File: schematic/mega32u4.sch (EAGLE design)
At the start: 28 parts, among them Q1 16 MHz, T1 BC847, X1 MINI-USB-32005-201

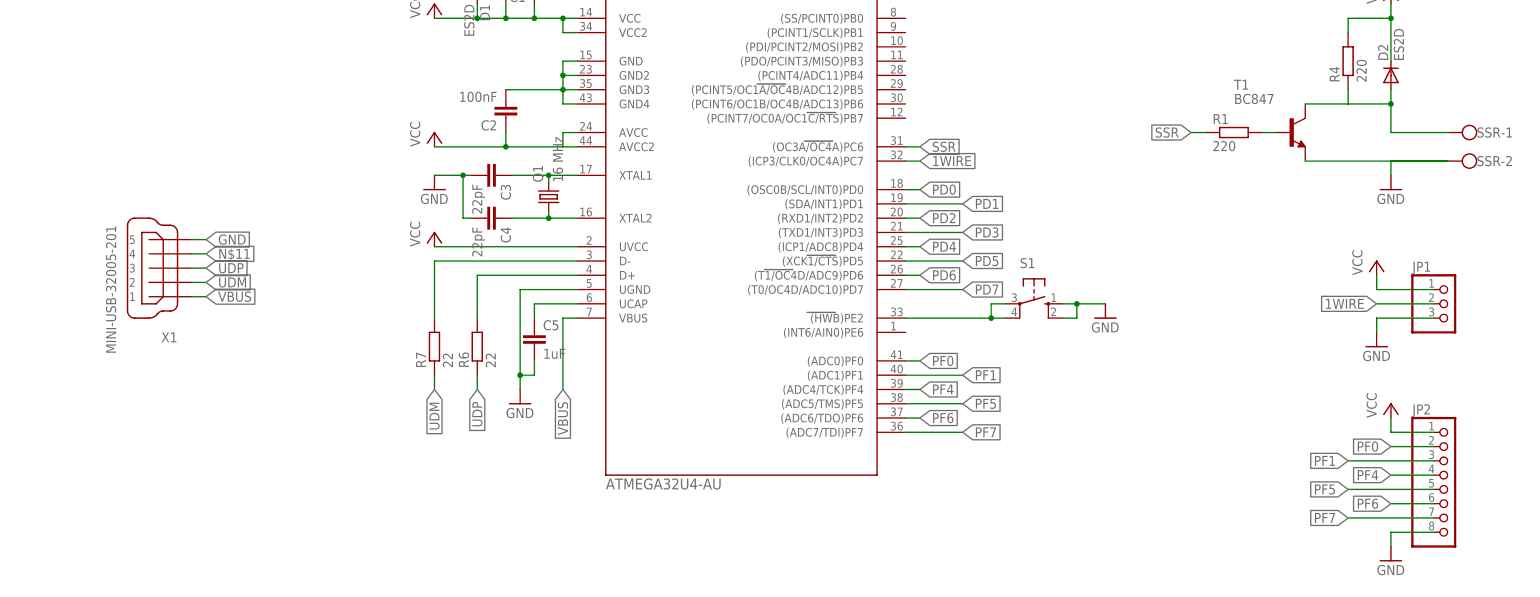
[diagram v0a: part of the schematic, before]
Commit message: Design Rule Check applied and errors corrected
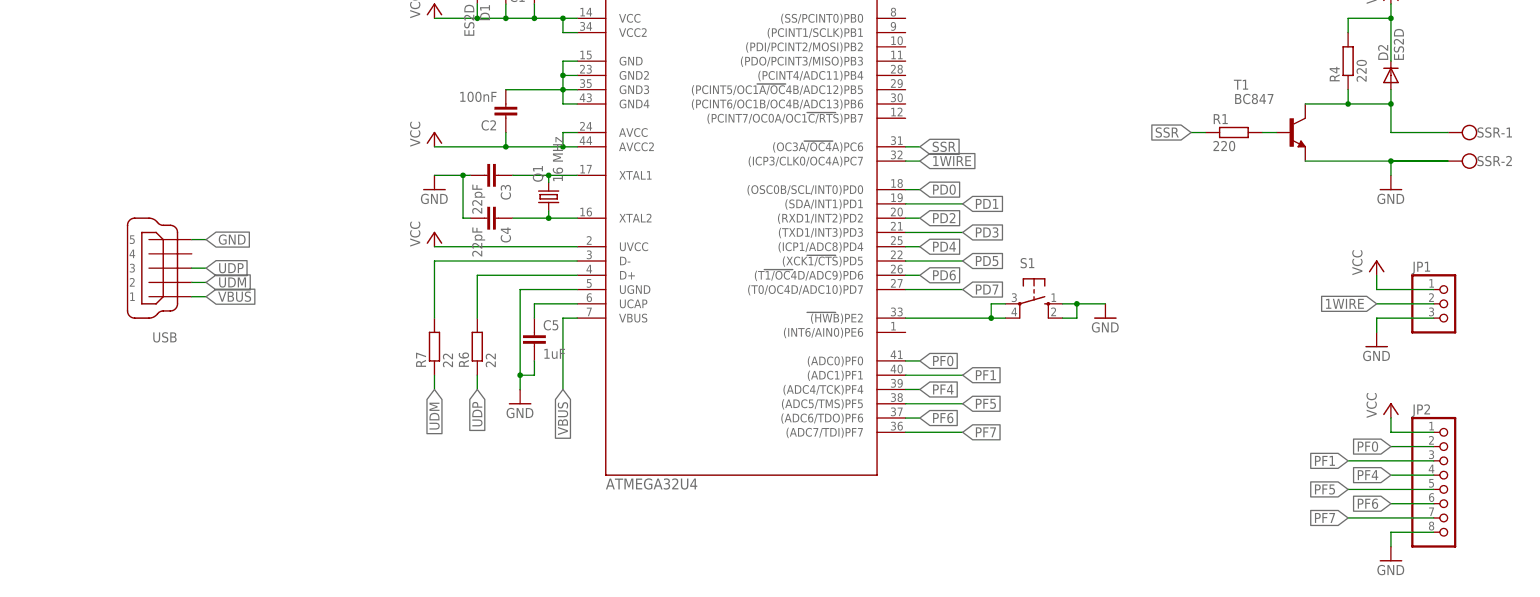
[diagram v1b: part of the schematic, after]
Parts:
- U$1: value ATMEGA32U4-AU -> ATMEGA32U4
- renumbered X1 to USB
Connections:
- removed net N$11: USB.4
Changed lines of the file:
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@@
 </classes>
 <parts>
-<part name="U$1" library="mega32U4" deviceset="ATMEGA32U4-AU" device=""/>
+<part name="U$1" library="mega32U4" deviceset="ATMEGA32U4-AU" device="" value="ATMEGA32U4"/>
 <part name="FRAME1" library="frames" deviceset="DINA3_L" device=""/>
 <part name="C1" library="resistor" deviceset="C-EU" device="C0805K" value="47nF"/>
@@
 <part name="GND6" library="supply1" deviceset="GND" device=""/>
 <part name="Q1" library="crystal" deviceset="CRYSTAL" device="CTS406" value="16 MHz"/>
-<part name="X1" library="con-cypressindustries" deviceset="MINI-USB-" device="32005-201"/>
+<part name="USB" library="con-cypressindustries" deviceset="MINI-USB-" device="32005-201" value=""/>
 <part name="S2" library="switch-omron" deviceset="10-XX" device="">
 <attribute name="MF" value=""/>
@@
 <instance part="GND6" gate="1" x="312.42" y="83.82"/>
 <instance part="Q1" gate="G$1" x="162.56" y="148.59" rot="R90"/>
-<instance part="X1" gate="G$1" x="93.98" y="135.89" rot="R180"/>
+<instance part="USB" gate="G$1" x="93.98" y="135.89" rot="R180"/>
 <instance part="S2" gate="1" x="95.25" y="198.12" rot="R270"/>
 <instance part="GND7" gate="1" x="80.01" y="193.04"/>
@@
 <wire x1="154.94" y1="160.02" x2="154.94" y2="157.48" width="0.1524" layer="91"/>
 <junction x="154.94" y="157.48"/>
+<junction x="165.1" y="157.48"/>
 </segment>
 <segment>
@@
 <pinref part="T1" gate="G$1" pin="E"/>
 <pinref part="SSR" gate="-2" pin="KL"/>
-<wire x1="297.18" y1="154.94" x2="322.58" y2="154.94" width="0.1524" layer="91"/>
+<wire x1="297.18" y1="154.94" x2="312.42" y2="154.94" width="0.1524" layer="91"/>
+<wire x1="312.42" y1="154.94" x2="322.58" y2="154.94" width="0.1524" layer="91"/>
 <wire x1="322.58" y1="154.94" x2="312.42" y2="154.94" width="0.1524" layer="91"/>
 <wire x1="312.42" y1="154.94" x2="312.42" y2="152.4" width="0.1524" layer="91"/>
 <pinref part="GND4" gate="1" pin="GND"/>
+<junction x="312.42" y="154.94"/>
 </segment>
 <segment>
@@
 </segment>
 <segment>
-<pinref part="X1" gate="G$1" pin="5"/>
+<pinref part="USB" gate="G$1" pin="5"/>
 <wire x1="99.06" y1="140.97" x2="101.6" y2="140.97" width="0.1524" layer="91"/>
 <label x="101.6" y="140.97" size="1.778" layer="95" xref="yes"/>
@@
 </segment>
 <segment>
-<pinref part="X1" gate="G$1" pin="2"/>
+<pinref part="USB" gate="G$1" pin="2"/>
 <wire x1="99.06" y1="133.35" x2="101.6" y2="133.35" width="0.1524" layer="91"/>
 <label x="101.6" y="133.35" size="1.778" layer="95" xref="yes"/>
@@
 </segment>
 <segment>
-<pinref part="X1" gate="G$1" pin="3"/>
+<pinref part="USB" gate="G$1" pin="3"/>
 <wire x1="99.06" y1="135.89" x2="101.6" y2="135.89" width="0.1524" layer="91"/>
 <label x="101.6" y="135.89" size="1.778" layer="95" xref="yes"/>
@@
 </segment>
 <segment>
-<pinref part="X1" gate="G$1" pin="1"/>
+<pinref part="USB" gate="G$1" pin="1"/>
 <wire x1="99.06" y1="130.81" x2="101.6" y2="130.81" width="0.1524" layer="91"/>
 <label x="101.6" y="130.81" size="1.778" layer="95" xref="yes"/>
@@
 <wire x1="312.42" y1="165.1" x2="312.42" y2="167.64" width="0.1524" layer="91"/>
 <junction x="312.42" y="165.1"/>
+<junction x="304.8" y="165.1"/>
 </segment>
 </net>
@@
 </segment>
 </net>
-<net name="N$11" class="0">
-<segment>
-<pinref part="X1" gate="G$1" pin="4"/>
-<wire x1="99.06" y1="138.43" x2="101.6" y2="138.43" width="0.1524" layer="91"/>
-<label x="101.6" y="138.43" size="1.778" layer="95" xref="yes"/>
-</segment>
-</net>

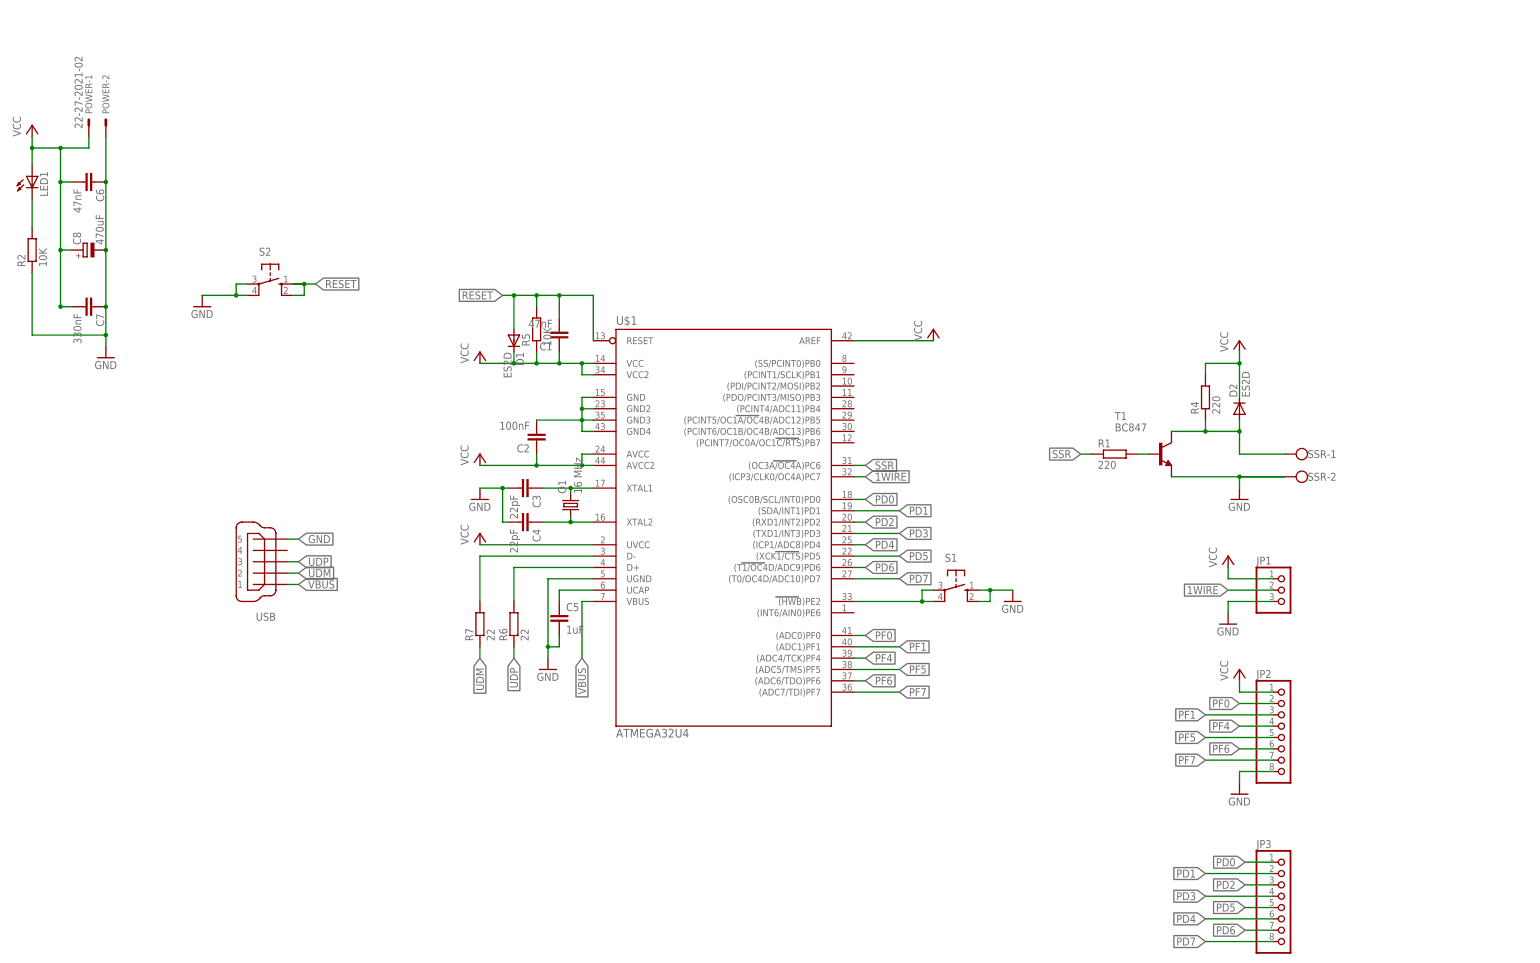
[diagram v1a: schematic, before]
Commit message: RGB-Led added, pin header repositioned, mounting holes added, ...
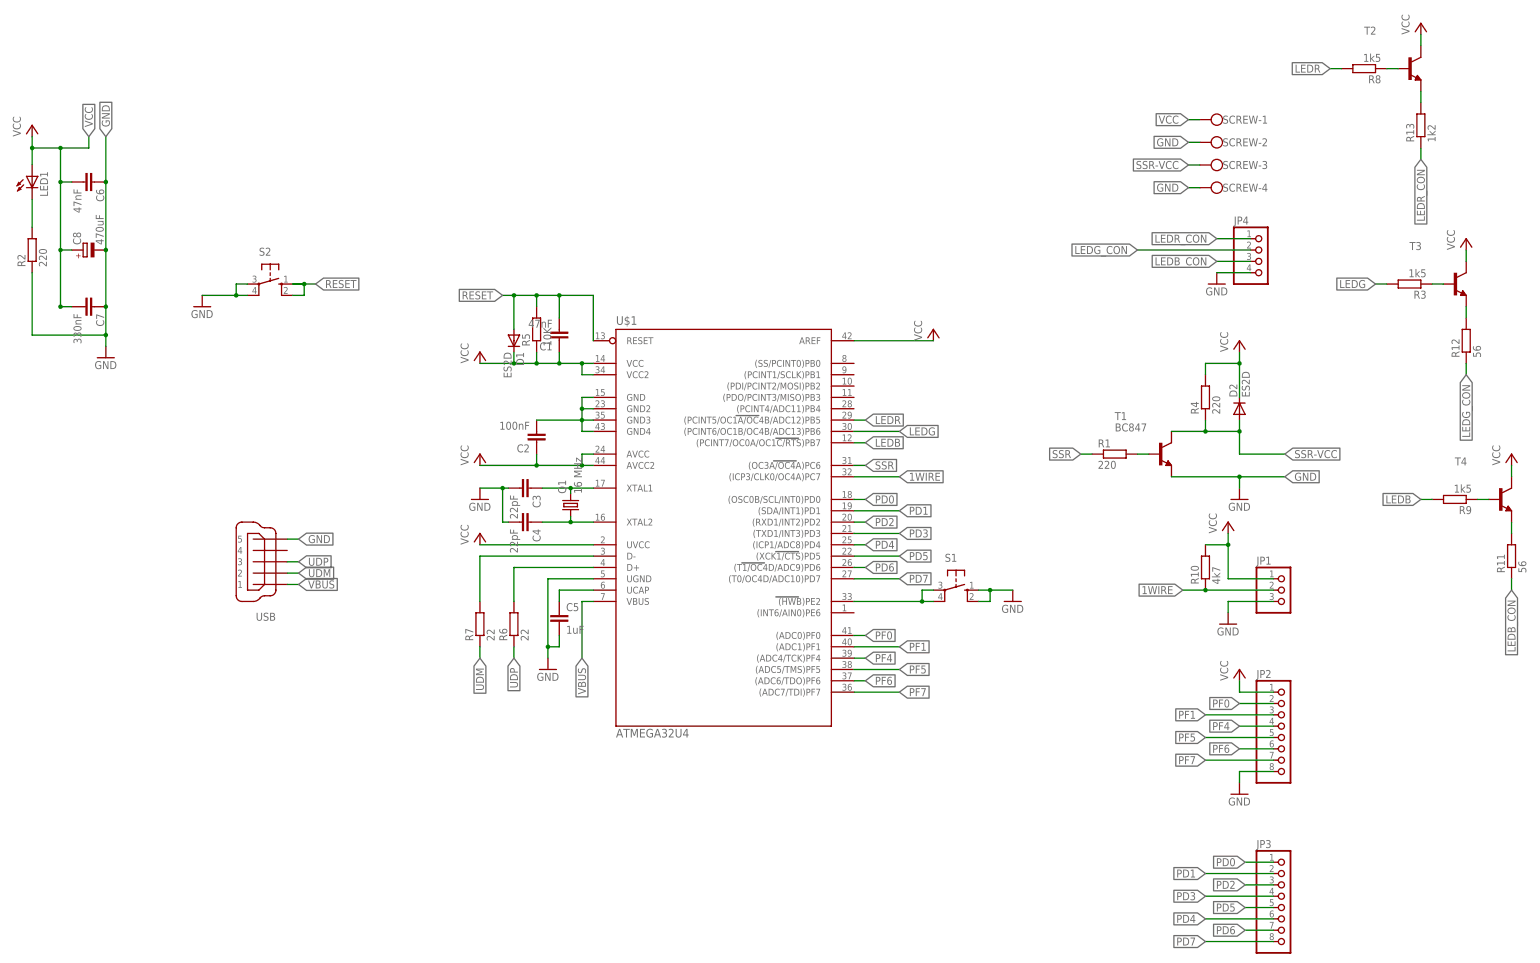
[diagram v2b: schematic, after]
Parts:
- removed POWER: 22-27-2021-02, con-molex:22-27-2021-02
- removed SSR: (no value), con-wago-500:W237-102
- added JP4: (no value), pinhead:PINHD-1X4
- added R10: 4k7, resistor:R-EU_R0805
- added R11, R12: 56, resistor:R-EU_R0805
- added R13: 1k2, resistor:R-EU_R0805
- added R3, R8, R9: 1k5, resistor:R-EU_R0805
- added SCREW: (no value), con-wago-500:W237-4
- added T2, T3, T4: (no value), transistor-neu-to92:BC817-25-NPN-SOT23-BEC
- R2: value 10K -> 220
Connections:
- new net LEDB: R9.2, U$1.(PCINT7/OC0A/OC1C/RTS)PB7
- new net LEDB_CON: JP4.3, R11.1
- new net LEDG: R3.2, U$1.(PCINT6/OC1B/OC4B/ADC13)PB6
- new net LEDG_CON: JP4.2, R12.1
- new net LEDR: R8.2, U$1.(PCINT5/OC1A/OC4B/ADC12)PB5
- new net LEDR_CON: JP4.1, R13.1
- new net N$11: R9.1, T4.B
- new net N$14: R11.2, T4.E
- new net N$15: R12.2, T3.E
- new net N$16: R13.2, T2.E
- new net N$8: R8.1, T2.B
- new net SSR-VCC: D2.A, R4.1, SCREW-3.KL, T1.C
- net 1WIRE: now also R10.1
- net GND: now also JP4.4, SCREW-2.KL, SCREW-4.KL; no longer POWER-2.S, SSR-2.KL
- net N$9: now also R3.1, T3.B; no longer D2.A, R4.1, SSR-1.KL, T1.C
- net VCC: now also R10.2, SCREW-1.KL, T2.C, T3.C, T4.C; no longer POWER-1.S
